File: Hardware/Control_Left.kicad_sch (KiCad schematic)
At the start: 30 parts, among them J1 BAT, J2 TagConnect, J3 0.96_TFT_MODULE, Q1 AO3401A, Q2 AO3401A, SW1 MSK12C02, U1 TPS61040DBV, U2 XIAO-NRF52840-PLUS

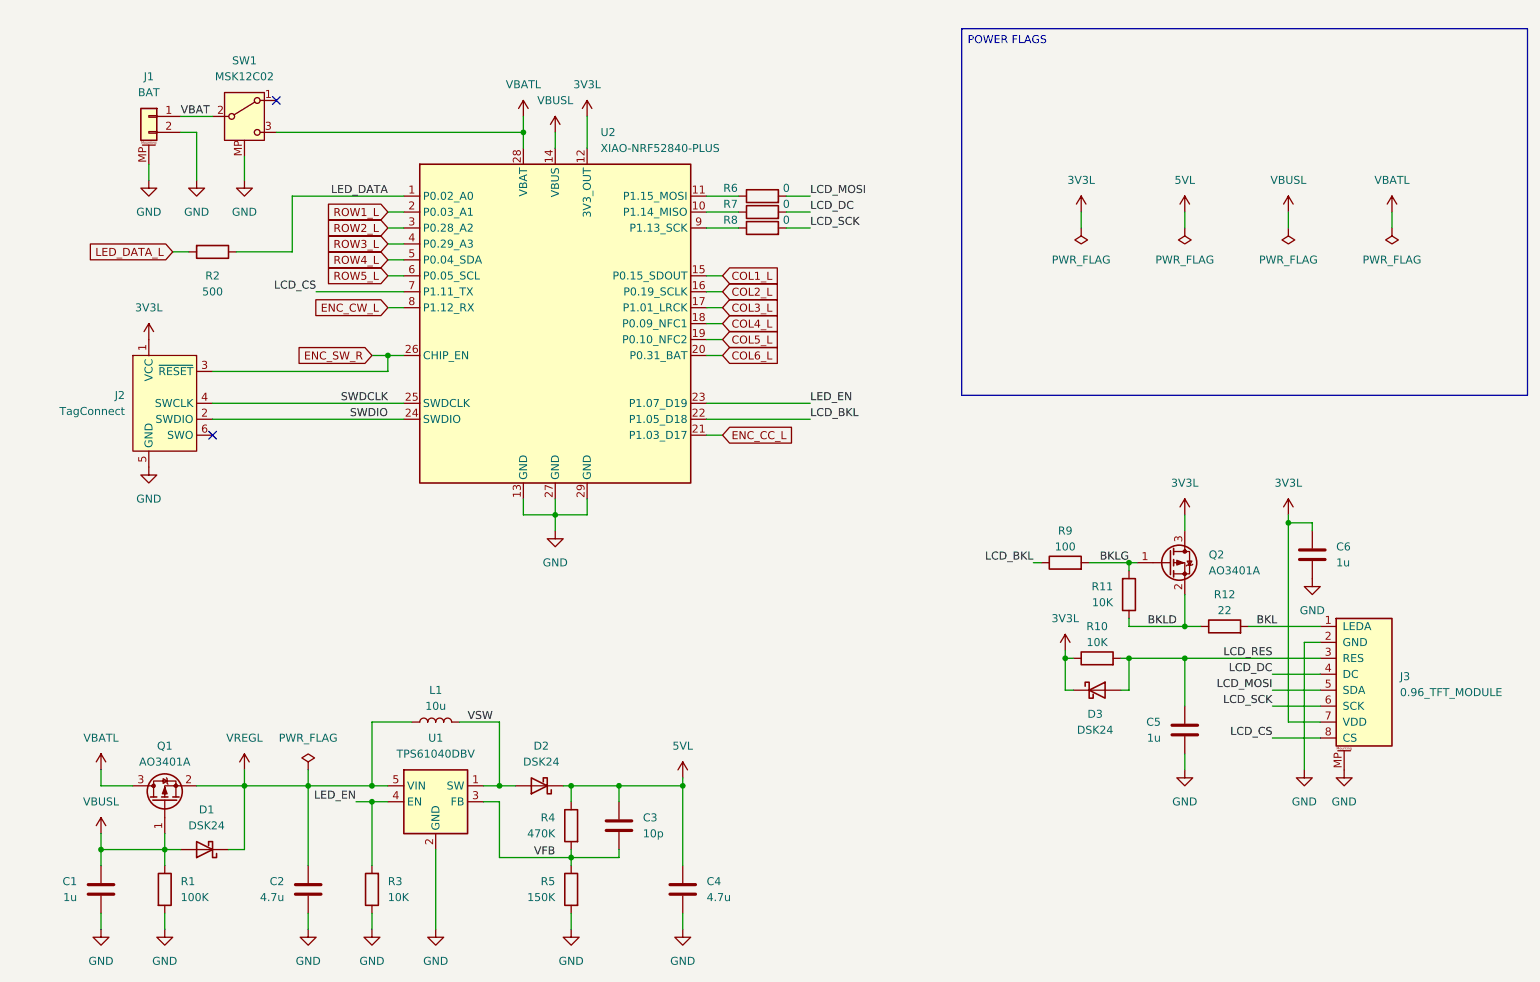
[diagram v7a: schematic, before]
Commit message: Reset button and LED switch
Added an LED power switch.
Returned the reset button for bootloader access.
Focus on changing the display to an e-ink one for lower power consumption.
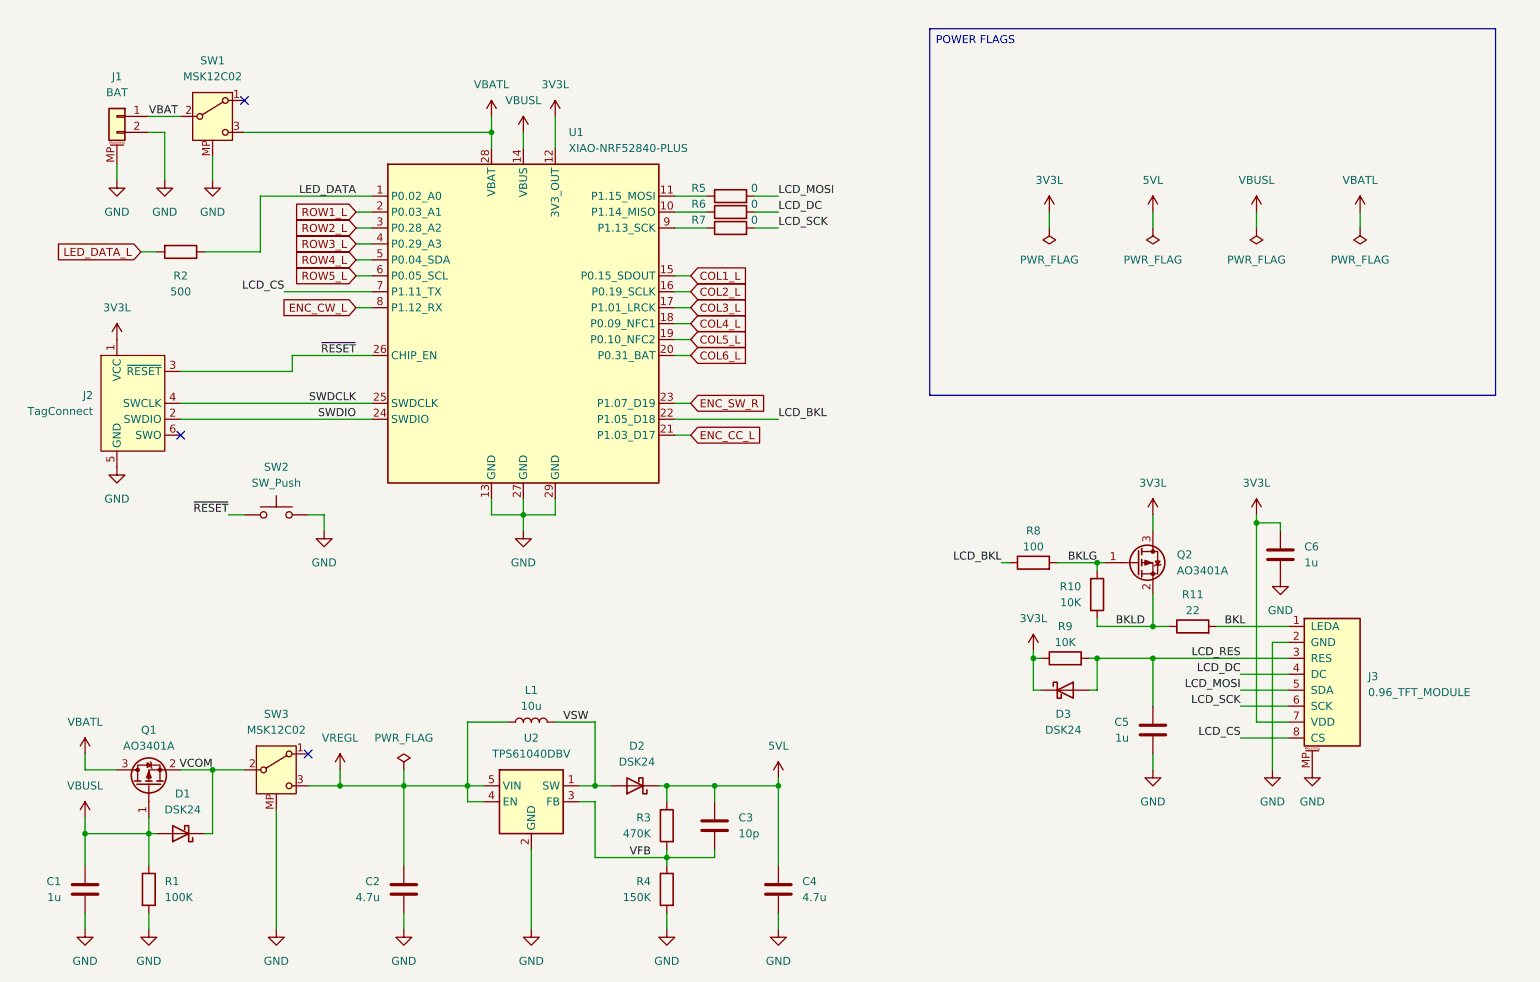
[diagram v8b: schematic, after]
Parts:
- removed R3: 10K, Resistor_SMD:R_0603_1608Metric, symbol Device:R
- added SW2: SW_Push, Button_Switch_SMD:SW_SPST_TS-1088-xR020, symbol Switch:SW_Push
- added SW3: MSK12C02, Custom_Parts:MSK12C02, symbol Custom_Parts:MSK12C02
- renumbered R11 to R10, R12 to R11, R4 to R3, R5 to R4, R6 to R5, R7 to R6, R8 to R7, R9 to R8, R10 to R9, U2 to U1, U1 to U2
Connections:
- net ENC_SW_R: now also U1.23 (P1.07_D19); no longer J2.3 (~{RESET}), U1.26 (CHIP_EN)
- net GND: now also SW2.2, SW3.MP
- net VREGL: now also U2.4 (EN), SW3.3 (C); no longer D1.1 (K), Q1.2 (S)
- removed net LED_EN: U1.23 (P1.07_D19), U2.4 (EN)
- new net VCOM: D1.1 (K), Q1.2 (S), SW3.2 (B)
- new net ~{RESET}: J2.3 (~{RESET}), SW2.1, U1.26 (CHIP_EN)
- no-connect marks 2 -> 3
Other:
- moved on the sheet: C1, C2, C3, C4, C5, C6, D1, D2, D3, J1, J2, J3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
